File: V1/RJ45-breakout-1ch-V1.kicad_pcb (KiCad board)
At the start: 2 copper layers, 110 x 100 mm, 37 parts, among them J1 RJ45, J2 SWITCHES

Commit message: Footprints updated
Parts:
- removed ?: , Tales:Grandmas_small
- removed FID1, FID2, FID3, FID4, FID5, FID6: Fiducial_1mm_Mask2mm, Fiducial:Fiducial_1mm_Mask2mm
- J1 (x15): footprint Tales:RJ45_Amphenol_RJHSE5080 -> Tales:RJ45_CKMTW_R-RJ45R08P-A004
- moved J2 8.00 mm to (186.4, 134.1)
- moved J2 8.00 mm to (98.4, 134.1)
- moved J2 8.00 mm to (164.4, 134.1)
- moved J2 8.00 mm to (142.4, 134.1)
- moved J2 8.00 mm to (120.4, 134.1)
- moved J1 8.00 mm to (102.2, 120.1)
- moved J1 8.00 mm to (146.2, 92.1)
- moved J1 8.00 mm to (124.2, 120.1)
- moved J1 8.00 mm to (124.2, 92.1)
- moved J1 8.00 mm to (190.2, 120.1)
- moved J1 8.00 mm to (190.2, 92.1)
- moved J1 8.00 mm to (102.2, 92.1)
- moved J1 8.00 mm to (168.2, 120.1)
- moved J1 8.00 mm to (168.2, 92.1)
- moved J1 8.00 mm to (146.2, 120.1)
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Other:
- board size 110 x 100 mm -> 110 x 84 mm
- board text added: "V-CUT"
- board text removed: "1X RJ45 BREAKOUT"
- board text removed: "Grandma's House"
- board text removed: "Home Automation"

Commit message: PCB adjustments
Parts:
- turned J1 to 180 degrees (x15)

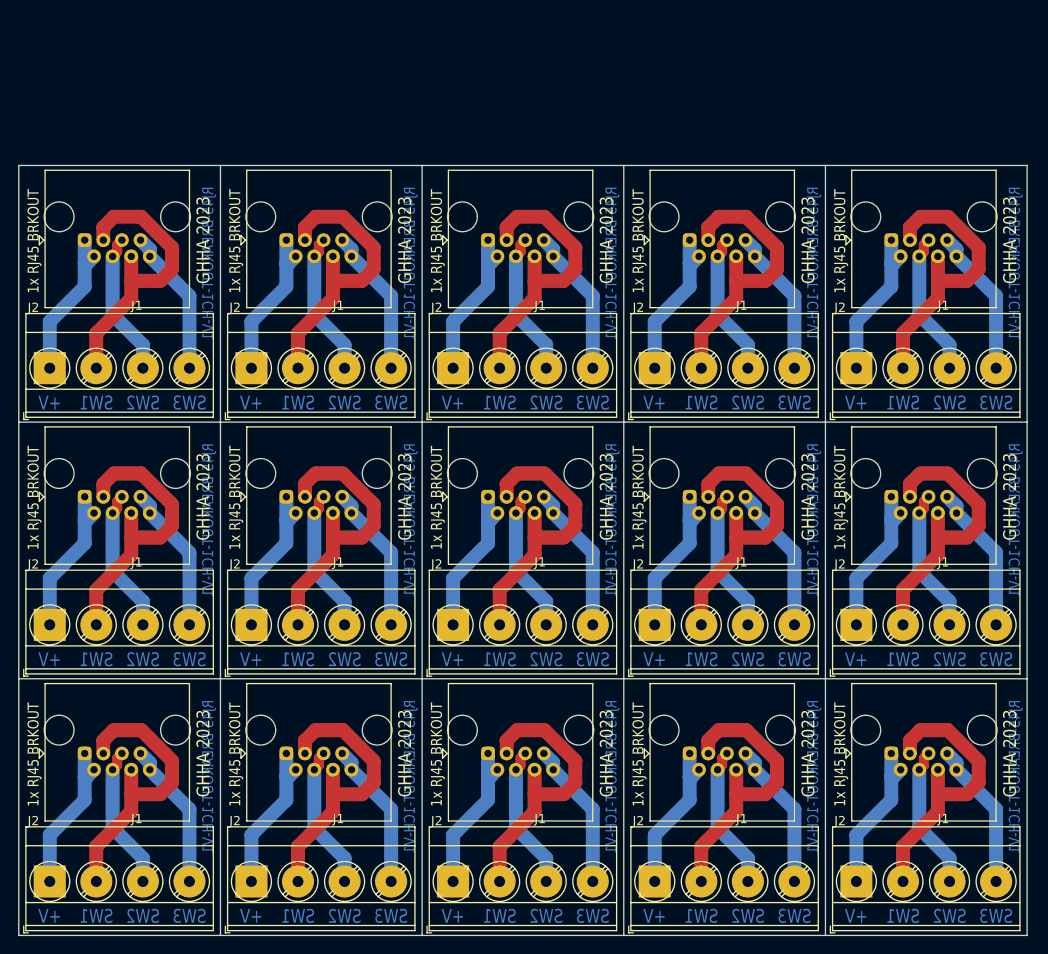
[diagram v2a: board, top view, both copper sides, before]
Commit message: Align parts and tracks to mm grid
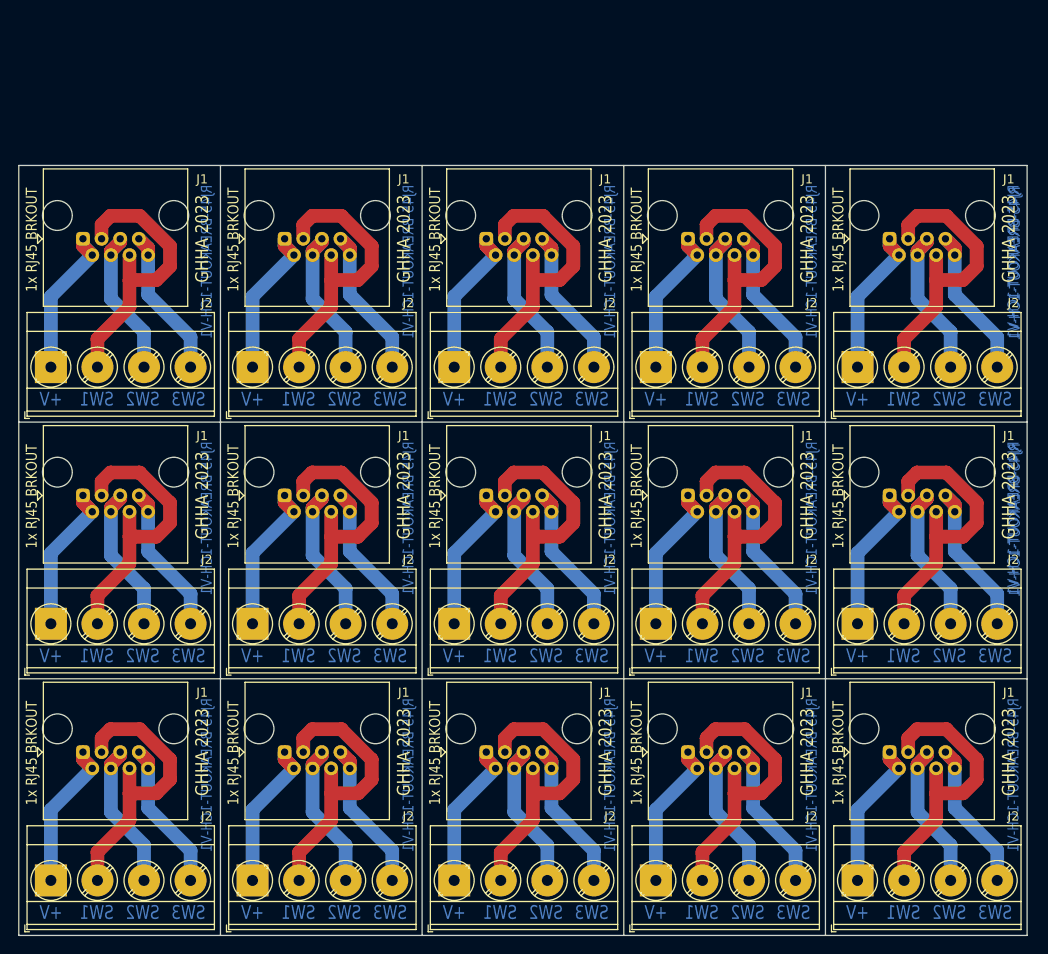
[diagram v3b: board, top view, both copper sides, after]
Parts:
- removed the J1 at (146.2, 92.1)
- removed the J1 at (124.2, 120.1)
- removed the J1 at (102.2, 64.1)
- removed the J1 at (124.2, 92.1)
- removed the J1 at (168.2, 64.1)
- removed the J1 at (190.2, 120.1)
- removed the J1 at (190.2, 64.1)
- removed the J1 at (146.2, 64.1)
- removed the J1 at (190.2, 92.1)
- removed the J1 at (102.2, 92.1)
- removed the J1 at (168.2, 120.1)
- removed the J1 at (168.2, 92.1)
- removed the J1 at (146.2, 120.1)
- removed the J1 at (124.2, 64.1)
- removed the J2 at (186.4, 134.1)
- removed the J2 at (164.4, 78.1)
- removed the J2 at (164.4, 134.1)
- removed the J2 at (98.4, 106.1)
- removed the J2 at (186.4, 78.1)
- removed the J2 at (186.4, 106.1)
- removed the J2 at (98.4, 78.1)
- removed the J2 at (142.4, 134.1)
- removed the J2 at (164.4, 106.1)
- removed the J2 at (120.4, 134.1)
- removed the J2 at (142.4, 78.1)
- removed the J2 at (142.4, 106.1)
- removed the J2 at (120.4, 106.1)
- removed the J2 at (120.4, 78.1)
- added J1: RJ45, Tales:RJ45_CKMTW_R-RJ45R08P-A004, F.Cu at (168.0, 64.0)
- added J1: RJ45, Tales:RJ45_CKMTW_R-RJ45R08P-A004, F.Cu at (124.0, 64.0)
- added J1: RJ45, Tales:RJ45_CKMTW_R-RJ45R08P-A004, F.Cu at (190.0, 64.0)
- added J1: RJ45, Tales:RJ45_CKMTW_R-RJ45R08P-A004, F.Cu at (168.0, 92.0)
- added J1: RJ45, Tales:RJ45_CKMTW_R-RJ45R08P-A004, F.Cu at (102.0, 92.0)
- added J1: RJ45, Tales:RJ45_CKMTW_R-RJ45R08P-A004, F.Cu at (146.0, 92.0)
- added J1: RJ45, Tales:RJ45_CKMTW_R-RJ45R08P-A004, F.Cu at (146.0, 120.0)
- added J1: RJ45, Tales:RJ45_CKMTW_R-RJ45R08P-A004, F.Cu at (146.0, 64.0)
- added J1: RJ45, Tales:RJ45_CKMTW_R-RJ45R08P-A004, F.Cu at (102.0, 64.0)
- added J1: RJ45, Tales:RJ45_CKMTW_R-RJ45R08P-A004, F.Cu at (190.0, 92.0)
- added J1: RJ45, Tales:RJ45_CKMTW_R-RJ45R08P-A004, F.Cu at (124.0, 92.0)
- added J1: RJ45, Tales:RJ45_CKMTW_R-RJ45R08P-A004, F.Cu at (168.0, 120.0)
- added J1: RJ45, Tales:RJ45_CKMTW_R-RJ45R08P-A004, F.Cu at (190.0, 120.0)
- added J1: RJ45, Tales:RJ45_CKMTW_R-RJ45R08P-A004, F.Cu at (124.0, 120.0)
- added J2: SWITCHES, Tales:TerminalBlock_Phoenix_MKDS-3-4-5.08_1x04_P5.08mm_Horizontal, F.Cu at (164.5, 106.0)
- added J2: SWITCHES, Tales:TerminalBlock_Phoenix_MKDS-3-4-5.08_1x04_P5.08mm_Horizontal, F.Cu at (98.5, 78.0)
- added J2: SWITCHES, Tales:TerminalBlock_Phoenix_MKDS-3-4-5.08_1x04_P5.08mm_Horizontal, F.Cu at (186.5, 78.0)
- added J2: SWITCHES, Tales:TerminalBlock_Phoenix_MKDS-3-4-5.08_1x04_P5.08mm_Horizontal, F.Cu at (186.5, 106.0)
- added J2: SWITCHES, Tales:TerminalBlock_Phoenix_MKDS-3-4-5.08_1x04_P5.08mm_Horizontal, F.Cu at (120.5, 106.0)
- added J2: SWITCHES, Tales:TerminalBlock_Phoenix_MKDS-3-4-5.08_1x04_P5.08mm_Horizontal, F.Cu at (142.5, 78.0)
- added J2: SWITCHES, Tales:TerminalBlock_Phoenix_MKDS-3-4-5.08_1x04_P5.08mm_Horizontal, F.Cu at (142.5, 106.0)
- added J2: SWITCHES, Tales:TerminalBlock_Phoenix_MKDS-3-4-5.08_1x04_P5.08mm_Horizontal, F.Cu at (164.5, 134.0)
- added J2: SWITCHES, Tales:TerminalBlock_Phoenix_MKDS-3-4-5.08_1x04_P5.08mm_Horizontal, F.Cu at (164.5, 78.0)
- added J2: SWITCHES, Tales:TerminalBlock_Phoenix_MKDS-3-4-5.08_1x04_P5.08mm_Horizontal, F.Cu at (98.5, 106.0)
- added J2: SWITCHES, Tales:TerminalBlock_Phoenix_MKDS-3-4-5.08_1x04_P5.08mm_Horizontal, F.Cu at (120.5, 134.0)
- added J2: SWITCHES, Tales:TerminalBlock_Phoenix_MKDS-3-4-5.08_1x04_P5.08mm_Horizontal, F.Cu at (120.5, 78.0)
- added J2: SWITCHES, Tales:TerminalBlock_Phoenix_MKDS-3-4-5.08_1x04_P5.08mm_Horizontal, F.Cu at (186.5, 134.0)
- added J2: SWITCHES, Tales:TerminalBlock_Phoenix_MKDS-3-4-5.08_1x04_P5.08mm_Horizontal, F.Cu at (142.5, 134.0)
- moved J1 0.24 mm to (102.0, 120.0)
- moved J2 0.17 mm to (98.5, 134.0)
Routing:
- net Net-(J2-Pin_4): track 242.7 -> 278.1 mm
- net Net-(J2-Pin_1): track 253.2 -> 277.4 mm
- net Net-(J2-Pin_2): track 477.8 -> 475.2 mm
- net Net-(J2-Pin_3): track 269.4 -> 271.8 mm

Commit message: Something...
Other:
- board text added: "GH2023"
- board text removed: "GHHA 2023"
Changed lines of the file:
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@@
     (effects (font (size 1.2 1) (thickness 0.2)) (justify mirror))
   )
-  (gr_text "GHHA 2023" (at 159 92 90) (layer "F.SilkS")
+  (gr_text "GH2023" (at 159 92 90) (layer "F.SilkS")
     (effects (font (size 1.4 1.2) (thickness 0.2)))
   )
-  (gr_text "GHHA 2023" (at 115 92 90) (layer "F.SilkS")
+  (gr_text "GH2023" (at 115 92 90) (layer "F.SilkS")
     (effects (font (size 1.4 1.2) (thickness 0.2)))
   )
   (gr_text "1x RJ45 BRKOUT" (at 162.4 120.1 90) (layer "F.SilkS")
-    (effects (font (size 1.2 1) (thickness 0.2)))
+    (effects (font (size 1.4 1.2) (thickness 0.2)))
   )
   (gr_text "1x RJ45 BRKOUT" (at 184.4 92.1 90) (layer "F.SilkS")
-    (effects (font (size 1.2 1) (thickness 0.2)))
-  )
-  (gr_text "GHHA 2023" (at 181 120 90) (layer "F.SilkS")
     (effects (font (size 1.4 1.2) (thickness 0.2)))
   )
-  (gr_text "GHHA 2023" (at 137 64 90) (layer "F.SilkS")
+  (gr_text "GH2023" (at 181 120 90) (layer "F.SilkS")
     (effects (font (size 1.4 1.2) (thickness 0.2)))
   )
-  (gr_text "GHHA 2023" (at 181 64 90) (layer "F.SilkS")
+  (gr_text "GH2023" (at 137 64 90) (layer "F.SilkS")
+    (effects (font (size 1.4 1.2) (thickness 0.2)))
+  )
+  (gr_text "GH2023" (at 181 64 90) (layer "F.SilkS")
     (effects (font (size 1.4 1.2) (thickness 0.2)))
   )
   (gr_text "1x RJ45 BRKOUT" (at 162.4 64.1 90) (layer "F.SilkS")
-    (effects (font (size 1.2 1) (thickness 0.2)))
+    (effects (font (size 1.4 1.2) (thickness 0.2)))
   )
-  (gr_text "GHHA 2023" (at 203 64 90) (layer "F.SilkS")
+  (gr_text "GH2023" (at 203 64 90) (layer "F.SilkS")
     (effects (font (size 1.4 1.2) (thickness 0.2)))
   )
   (gr_text "1x RJ45 BRKOUT" (at 96.4 64.1 90) (layer "F.SilkS")
-    (effects (font (size 1.2 1) (thickness 0.2)))
+    (effects (font (size 1.4 1.2) (thickness 0.2) bold))
   )
   (gr_text "1x RJ45 BRKOUT" (at 140.4 92.1 90) (layer "F.SilkS")
-    (effects (font (size 1.2 1) (thickness 0.2)))
+    (effects (font (size 1.4 1.2) (thickness 0.2)))
   )
   (gr_text "1x RJ45 BRKOUT" (at 140.4 64.1 90) (layer "F.SilkS")
-    (effects (font (size 1.2 1) (thickness 0.2)))
+    (effects (font (size 1.4 1.2) (thickness 0.2)))
   )
   (gr_text "1x RJ45 BRKOUT" (at 162.4 92.1 90) (layer "F.SilkS")
-    (effects (font (size 1.2 1) (thickness 0.2)))
+    (effects (font (size 1.4 1.2) (thickness 0.2)))
   )
   (gr_text "1x RJ45 BRKOUT" (at 118.4 120.1 90) (layer "F.SilkS")
-    (effects (font (size 1.2 1) (thickness 0.2)))
+    (effects (font (size 1.4 1.2) (thickness 0.2)))
   )
   (gr_text "1x RJ45 BRKOUT" (at 118.4 92.1 90) (layer "F.SilkS")
-    (effects (font (size 1.2 1) (thickness 0.2)))
+    (effects (font (size 1.4 1.2) (thickness 0.2)))
   )
   (gr_text "1x RJ45 BRKOUT" (at 184.4 64.1 90) (layer "F.SilkS")
-    (effects (font (size 1.2 1) (thickness 0.2)))
+    (effects (font (size 1.4 1.2) (thickness 0.2)))
   )
   (gr_text "1x RJ45 BRKOUT" (at 184.4 120.1 90) (layer "F.SilkS")
-    (effects (font (size 1.2 1) (thickness 0.2)))
+    (effects (font (size 1.4 1.2) (thickness 0.2)))
   )
   (gr_text "1x RJ45 BRKOUT" (at 96.4 120.1 90) (layer "F.SilkS")
-    (effects (font (size 1.2 1) (thickness 0.2)))
+    (effects (font (size 1.4 1.2) (thickness 0.2)))
   )
   (gr_text "1x RJ45 BRKOUT" (at 140.4 120.1 90) (layer "F.SilkS")
-    (effects (font (size 1.2 1) (thickness 0.2)))
-  )
-  (gr_text "GHHA 2023" (at 115 120 90) (layer "F.SilkS")
     (effects (font (size 1.4 1.2) (thickness 0.2)))
   )
-  (gr_text "GHHA 2023" (at 137 120 90) (layer "F.SilkS")
+  (gr_text "GH2023" (at 115 120 90) (layer "F.SilkS")
     (effects (font (size 1.4 1.2) (thickness 0.2)))
   )
-  (gr_text "GHHA 2023" (at 181 92 90) (layer "F.SilkS")
+  (gr_text "GH2023" (at 137 120 90) (layer "F.SilkS")
     (effects (font (size 1.4 1.2) (thickness 0.2)))
   )
-  (gr_text "GHHA 2023" (at 203 92 90) (layer "F.SilkS")
+  (gr_text "GH2023" (at 181 92 90) (layer "F.SilkS")
     (effects (font (size 1.4 1.2) (thickness 0.2)))
   )
-  (gr_text "GHHA 2023" (at 159 64 90) (layer "F.SilkS")
+  (gr_text "GH2023" (at 203 92 90) (layer "F.SilkS")
+    (effects (font (size 1.4 1.2) (thickness 0.2)))
+  )
+  (gr_text "GH2023" (at 159 64 90) (layer "F.SilkS")
     (effects (font (size 1.4 1.2) (thickness 0.2)))
   )
   (gr_text "1x RJ45 BRKOUT" (at 118.4 64.1 90) (layer "F.SilkS")
-    (effects (font (size 1.2 1) (thickness 0.2)))
-  )
-  (gr_text "GHHA 2023" (at 137 92 90) (layer "F.SilkS")
     (effects (font (size 1.4 1.2) (thickness 0.2)))
   )
-  (gr_text "GHHA 2023" (at 115 64 90) (layer "F.SilkS")
+  (gr_text "GH2023" (at 137 92 90) (layer "F.SilkS")
     (effects (font (size 1.4 1.2) (thickness 0.2)))
   )
-  (gr_text "GHHA 2023" (at 159 120 90) (layer "F.SilkS")
+  (gr_text "GH2023" (at 115 64 90) (layer "F.SilkS")
     (effects (font (size 1.4 1.2) (thickness 0.2)))
   )
-  (gr_text "GHHA 2023" (at 203 120 90) (layer "F.SilkS")
+  (gr_text "GH2023" (at 159 120 90) (layer "F.SilkS")
+    (effects (font (size 1.4 1.2) (thickness 0.2)))
+  )
+  (gr_text "GH2023" (at 203 120 90) (layer "F.SilkS")
     (effects (font (size 1.4 1.2) (thickness 0.2)))
   )
   (gr_text "1x RJ45 BRKOUT" (at 96.4 92.1 90) (layer "F.SilkS")
-    (effects (font (size 1.2 1) (thickness 0.2)))
+    (effects (font (size 1.4 1.2) (thickness 0.2)))
   )
   (gr_text "V-CUT" (at 180.5 50) (layer "Cmts.User")

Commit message: Texts position adjusted
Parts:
- removed the J2 at (164.5, 106.0)
- removed the J2 at (98.5, 78.0)
- removed the J2 at (186.5, 78.0)
- removed the J2 at (186.5, 106.0)
- removed the J2 at (120.5, 106.0)
- removed the J2 at (142.5, 78.0)
- removed the J2 at (142.5, 106.0)
- removed the J2 at (164.5, 134.0)
- removed the J2 at (164.5, 78.0)
- removed the J2 at (98.5, 106.0)
- removed the J2 at (120.5, 134.0)
- removed the J2 at (120.5, 78.0)
- removed the J2 at (186.5, 134.0)
- removed the J2 at (142.5, 134.0)
- added J2: SWITCHES, Tales:TerminalBlock_Dibo_DB128L-5.08-4P_1x04_P5.08mm_Horizontal, F.Cu at (164.5, 106.0)
- added J2: SWITCHES, Tales:TerminalBlock_Dibo_DB128L-5.08-4P_1x04_P5.08mm_Horizontal, F.Cu at (120.5, 78.0)
- added J2: SWITCHES, Tales:TerminalBlock_Dibo_DB128L-5.08-4P_1x04_P5.08mm_Horizontal, F.Cu at (186.5, 134.0)
- added J2: SWITCHES, Tales:TerminalBlock_Dibo_DB128L-5.08-4P_1x04_P5.08mm_Horizontal, F.Cu at (164.5, 78.0)
- added J2: SWITCHES, Tales:TerminalBlock_Dibo_DB128L-5.08-4P_1x04_P5.08mm_Horizontal, F.Cu at (120.5, 106.0)
- added J2: SWITCHES, Tales:TerminalBlock_Dibo_DB128L-5.08-4P_1x04_P5.08mm_Horizontal, F.Cu at (186.5, 78.0)
- added J2: SWITCHES, Tales:TerminalBlock_Dibo_DB128L-5.08-4P_1x04_P5.08mm_Horizontal, F.Cu at (142.5, 78.0)
- added J2: SWITCHES, Tales:TerminalBlock_Dibo_DB128L-5.08-4P_1x04_P5.08mm_Horizontal, F.Cu at (142.5, 134.0)
- added J2: SWITCHES, Tales:TerminalBlock_Dibo_DB128L-5.08-4P_1x04_P5.08mm_Horizontal, F.Cu at (98.5, 106.0)
- added J2: SWITCHES, Tales:TerminalBlock_Dibo_DB128L-5.08-4P_1x04_P5.08mm_Horizontal, F.Cu at (164.5, 134.0)
- added J2: SWITCHES, Tales:TerminalBlock_Dibo_DB128L-5.08-4P_1x04_P5.08mm_Horizontal, F.Cu at (186.5, 106.0)
- added J2: SWITCHES, Tales:TerminalBlock_Dibo_DB128L-5.08-4P_1x04_P5.08mm_Horizontal, F.Cu at (142.5, 106.0)
- added J2: SWITCHES, Tales:TerminalBlock_Dibo_DB128L-5.08-4P_1x04_P5.08mm_Horizontal, F.Cu at (120.5, 134.0)
- added J2: SWITCHES, Tales:TerminalBlock_Dibo_DB128L-5.08-4P_1x04_P5.08mm_Horizontal, F.Cu at (98.5, 78.0)
- J2: footprint Tales:TerminalBlock_Phoenix_MKDS-3-4-5.08_1x04_P5.08mm_Horizontal -> Tales:TerminalBlock_Dibo_DB128L-5.08-4P_1x04_P5.08mm_Horizontal
- moved J1 0.50 mm to (102.5, 120.0)
- moved J1 0.50 mm to (168.5, 64.0)
- moved J1 0.50 mm to (124.5, 64.0)
- moved J1 0.50 mm to (190.5, 64.0)
- moved J1 0.50 mm to (168.5, 92.0)
- moved J1 0.50 mm to (102.5, 92.0)
- moved J1 0.50 mm to (146.5, 92.0)
- moved J1 0.50 mm to (146.5, 120.0)
- moved J1 0.50 mm to (146.5, 64.0)
- moved J1 0.50 mm to (102.5, 64.0)
- moved J1 0.50 mm to (190.5, 92.0)
- moved J1 0.50 mm to (124.5, 92.0)
- moved J1 0.50 mm to (168.5, 120.0)
- moved J1 0.50 mm to (190.5, 120.0)
- moved J1 0.50 mm to (124.5, 120.0)
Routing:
- net Net-(J2-Pin_2): track 475.2 -> 470.8 mm
- net Net-(J2-Pin_1): track 277.4 -> 280.5 mm
- net Net-(J2-Pin_4): track 278.1 -> 275.0 mm
- net Net-(J2-Pin_3): track 271.8 -> 268.7 mm
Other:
- board text added: "Grandma's House"
